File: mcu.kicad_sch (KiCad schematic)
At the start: 43 parts, among them J4 GPIO, J5 GND/3V3, Q3 MMBTA42, U4 STM32F103C8Tx, X1 SPI_DBG, X2 MTRBTN, X3 Bluetooth, X4 BuzzerHV, X5 BuzzerLV

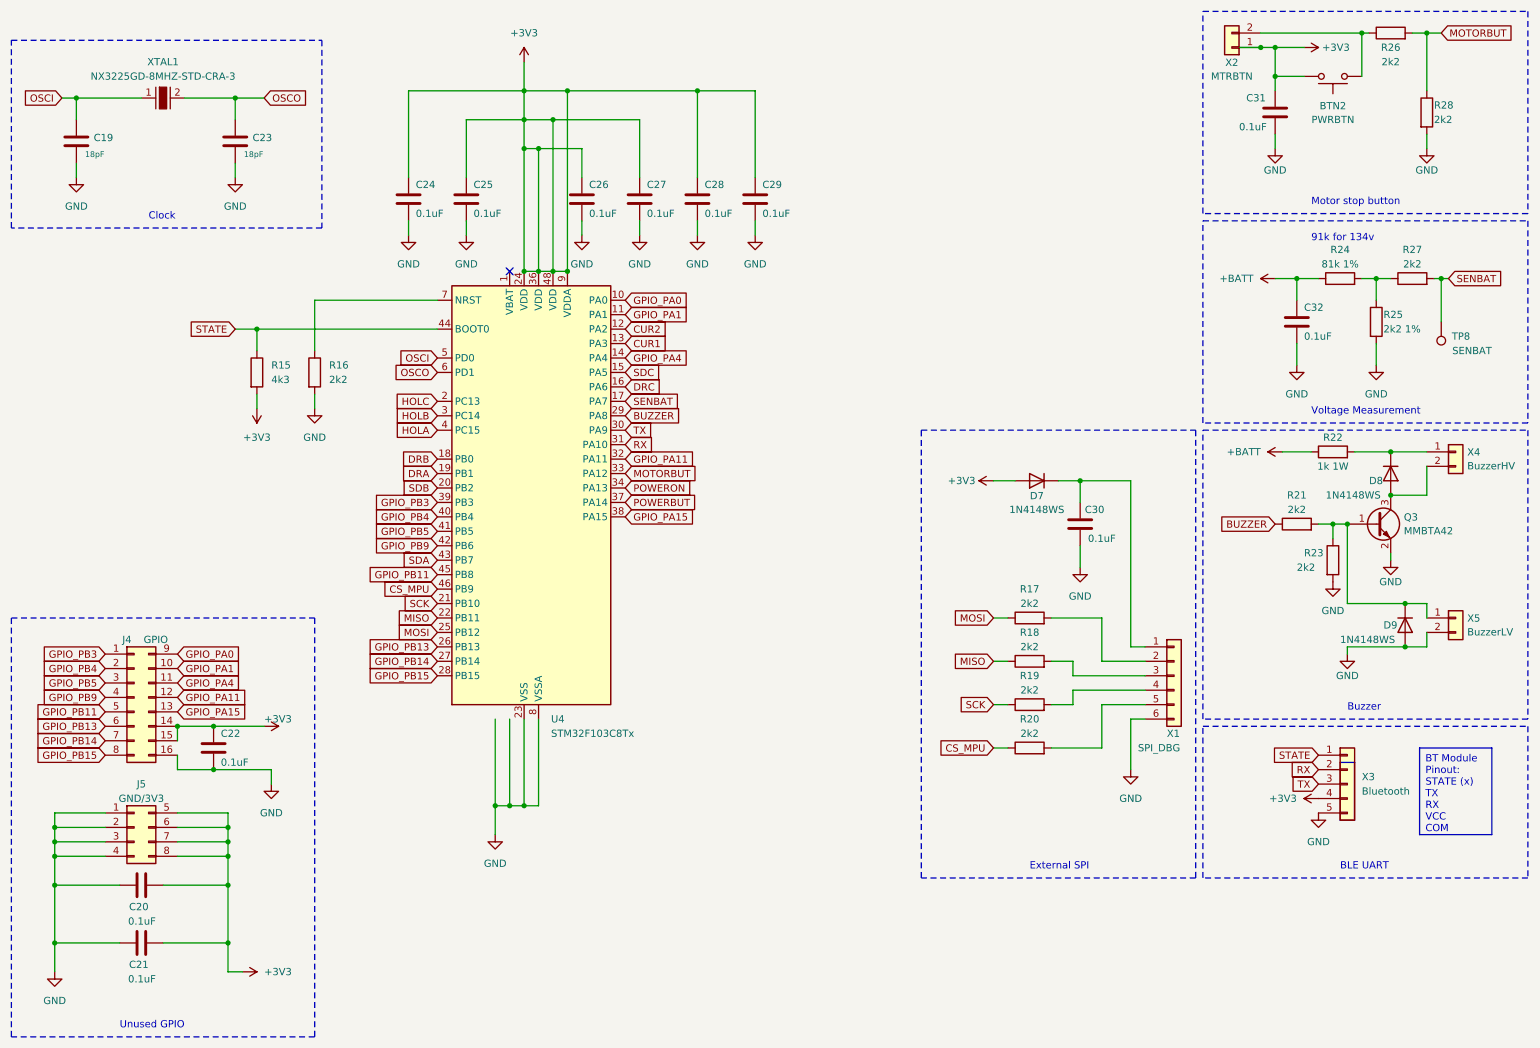
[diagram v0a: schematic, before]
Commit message: Add drivers, stepdown on VIPER115, fixes
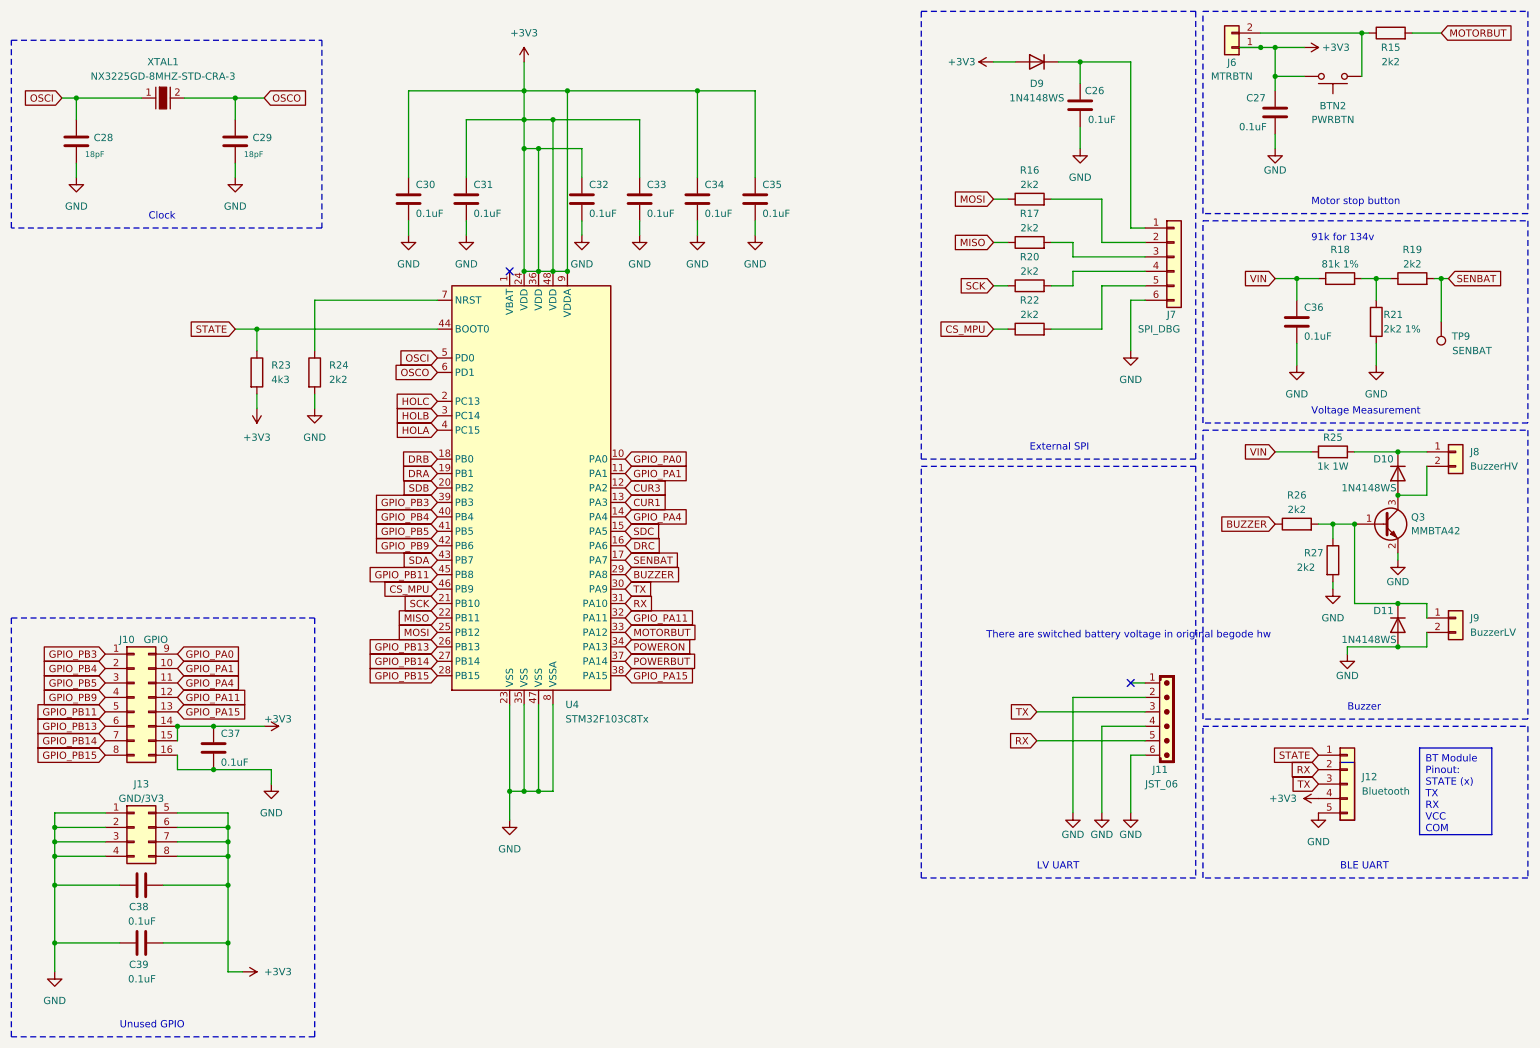
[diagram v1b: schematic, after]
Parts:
- removed D7, D8: 1N4148WS, Diode_SMD:D_SOD-323, symbol Diode:1N4148WS
- removed R28: 2k2, Resistor_SMD:R_0603_1608Metric_Pad0.98x0.95mm_HandSolder, symbol Device:R
- added D10, D11: 1N4148WS, Diode_SMD:D_SOD-323, symbol Diode:1N4148WS
- added J11: JST_06, Connector_JST:JST_EH_B6B-EH-A_1x06_P2.50mm_Vertical, symbol PCM_SL_Connectors:JST_06
- J12: renamed from X3; footprint (none) -> Connector_PinSocket_2.54mm:PinSocket_1x05_P2.54mm_Vertical
- J6: renamed from X2; footprint (none) -> Connector_JST:JST_XH_B2B-XH-A_1x02_P2.50mm_Vertical
- J7: renamed from X1; footprint (none) -> Connector_PinSocket_2.54mm:PinSocket_1x06_P2.54mm_Vertical
- J8: renamed from X4; footprint (none) -> Connector_JST:JST_XH_B2B-XH-A_1x02_P2.50mm_Vertical
- J9: renamed from X5; footprint (none) -> Connector_JST:JST_XH_B2B-XH-A_1x02_P2.50mm_Vertical
- renumbered C30 to C26, C31 to C27, C19 to C28, C23 to C29, C24 to C30, C25 to C31, C26 to C32, C27 to C33, C28 to C34, C29 to C35, C32 to C36, C22 to C37, C20 to C38, C21 to C39, J4 to J10, J5 to J13, R26 to R15, R17 to R16, R18 to R17, R24 to R18, R27 to R19, R19 to R20, R25 to R21, R20 to R22, R15 to R23, R16 to R24, R22 to R25, R21 to R26, R23 to R27, TP8 to TP9
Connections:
- net +3V3: now also D9.2 (A)
- net GND: now also D11.2 (A), J11.2, J11.4, J11.6; no longer D9.2 (A)
- net RX: now also J11.5
- net TX: now also J11.3
- net at C26.1, J7.1 (Pin_1): now also D9.1 (K)
- net at J8.1 (Pin_1), R25.2: now also D10.1 (K)
- net at J8.2 (Pin_2), Q3.3 (C): now also D10.2 (A)
- net at J9.1 (Pin_1), Q3.1 (B), R26.2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: now also D11.1 (K); no longer D9.1 (K)
- net +BATT renamed VIN
- net CUR2 renamed CUR3
- no-connect marks 1 -> 2
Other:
- note added: "LV UART"
- note added: "There are switched battery voltage in original begode hw"
- moved on the sheet: C26, J7, Q3, R16, R17, R20, R22

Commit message: topology in progress
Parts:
- added C57: 0.1uF, Capacitor_SMD:C_0805_2012Metric_Pad1.18x1.45mm_HandSolder, symbol Device:C
- C39: value 0.1uF -> 1uF
- R23: value 4k3 -> 4k7
- R25: value 1k 1W -> 1k5 1W
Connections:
- net +3V3: now also C57.1
- net GND: now also C57.2
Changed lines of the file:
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@@
   (junction (at 25.4 161.29) (diameter 0) (color 0 0 0 0)
   )
+  (junction (at 240.03 151.13) (diameter 0) (color 0 0 0 0)
+  )
   (junction (at 255.27 16.51) (diameter 0) (color 0 0 0 0)
   )
@@
   )
   (junction (at 25.4 158.75) (diameter 0) (color 0 0 0 0)
+  )
+  (junction (at 247.65 158.75) (diameter 0) (color 0 0 0 0)
   )
   (junction (at 29.21 27.94) (diameter 0) (color 0 0 0 0)
@@
     (stroke (width 0) (type default))
   )
+  (wire (pts (xy 240.03 158.75) (xy 247.65 158.75))
+    (stroke (width 0) (type default))
+  )
   (wire (pts (xy 25.4 153.67) (xy 25.4 156.21))
     (stroke (width 0) (type default))
@@
     (stroke (width 0) (type default))
   )
+  (wire (pts (xy 247.65 160.02) (xy 247.65 158.75))
+    (stroke (width 0) (type default))
+  )
   (wire (pts (xy 209.55 45.72) (xy 209.55 53.34))
     (stroke (width 0) (type default))
@@
     (stroke (width 0) (type default))
   )
+  (wire (pts (xy 247.65 158.75) (xy 247.65 153.67))
+    (stroke (width 0) (type default))
+  )
   (wire (pts (xy 25.4 181.61) (xy 25.4 176.53))
     (stroke (width 0) (type default))
@@
     (stroke (width 0) (type default))
   )
+  (wire (pts (xy 237.49 151.13) (xy 240.03 151.13))
+    (stroke (width 0) (type default))
+  )
   (wire (pts (xy 46.99 138.43) (xy 46.99 140.97))
     (stroke (width 0) (type default))
@@
   )
   (wire (pts (xy 55.88 181.61) (xy 55.88 176.53))
+    (stroke (width 0) (type default))
+  )
+  (wire (pts (xy 240.03 151.13) (xy 247.65 151.13))
     (stroke (width 0) (type default))
   )
@@
     (effects (font (size 1.27 1.27)) (justify left bottom))
   )
-  (text "There are switched battery voltage in original begode hw"
-    (at 189.23 123.19 0)
+  (text "There are switched battery voltage\nin original begode hw"
+    (at 190.5 130.81 0)
     (effects (font (size 1.27 1.27)) (justify left bottom))
   )
@@
     )
   )
-  (symbol (lib_id "power:GND") (at 247.65 153.67 0) (unit 1)
-    (in_bom yes) (on_board yes) (dnp no) (fields_autoplaced)
-    (property "Reference" "#PWR065" (at 247.65 160.02 0)
-      (effects (font (size 1.27 1.27)) hide)
-    )
-    (property "Value" "GND" (at 247.65 158.75 0)
-      (effects (font (size 1.27 1.27)))
-    )
-    (property "Footprint" "" (at 247.65 153.67 0)
-      (effects (font (size 1.27 1.27)) hide)
-    )
-    (property "Datasheet" "" (at 247.65 153.67 0)
+  (symbol (lib_id "power:GND") (at 247.65 160.02 0) (unit 1)
+    (in_bom yes) (on_board yes) (dnp no)
+    (property "Reference" "#PWR065" (at 247.65 166.37 0)
+      (effects (font (size 1.27 1.27)) hide)
+    )
+    (property "Value" "GND" (at 247.65 163.83 0)
+      (effects (font (size 1.27 1.27)))
+    )
+    (property "Footprint" "" (at 247.65 160.02 0)
+      (effects (font (size 1.27 1.27)) hide)
+    )
+    (property "Datasheet" "" (at 247.65 160.02 0)
       (effects (font (size 1.27 1.27)) hide)
     )
@@
       (effects (font (size 1.27 1.27)) (justify left))
     )
-    (property "Value" "4k3" (at 63.5 77.47 0)
+    (property "Value" "4k7" (at 63.5 77.47 0)
       (effects (font (size 1.27 1.27)) (justify left))
     )
@@
     )
   )
-  (symbol (lib_id "power:+3V3") (at 247.65 151.13 90) (unit 1)
+  (symbol (lib_id "power:+3V3") (at 237.49 151.13 90) (unit 1)
     (in_bom yes) (on_board yes) (dnp no) (fields_autoplaced)
-    (property "Reference" "#PWR061" (at 251.46 151.13 0)
-      (effects (font (size 1.27 1.27)) hide)
-    )
-    (property "Value" "+3V3" (at 243.84 151.13 90)
-      (effects (font (size 1.27 1.27)) (justify left))
-    )
-    (property "Footprint" "" (at 247.65 151.13 0)
-      (effects (font (size 1.27 1.27)) hide)
-    )
-    (property "Datasheet" "" (at 247.65 151.13 0)
+    (property "Reference" "#PWR061" (at 241.3 151.13 0)
+      (effects (font (size 1.27 1.27)) hide)
+    )
+    (property "Value" "+3V3" (at 233.68 151.13 90)
+      (effects (font (size 1.27 1.27)) (justify left))
+    )
+    (property "Footprint" "" (at 237.49 151.13 0)
+      (effects (font (size 1.27 1.27)) hide)
+    )
+    (property "Datasheet" "" (at 237.49 151.13 0)
       (effects (font (size 1.27 1.27)) hide)
     )
@@
         (path "/c57bc97c-1c43-4bb1-9424-fed846030b7b/013bb254-f239-4c32-8f76-0a97895c10b6"
           (reference "#PWR061") (unit 1)
+        )
+      )
+    )
+  )
+  (symbol (lib_id "Device:C") (at 240.03 154.94 0) (unit 1)
+    (in_bom yes) (on_board yes) (dnp no)
+    (property "Reference" "C57" (at 241.3 152.4 0)
+      (effects (font (size 1.27 1.27)) (justify left))
+    )
+    (property "Value" "0.1uF" (at 241.3 157.48 0)
+      (effects (font (size 1.27 1.27)) (justify left))
+    )
+    (property "Footprint" "Capacitor_SMD:C_0805_2012Metric_Pad1.18x1.45mm_HandSolder" (at 240.9952 158.75 0)
+      (effects (font (size 1.27 1.27)) hide)
+    )
+    (property "Datasheet" "~" (at 240.03 154.94 0)
+      (effects (font (size 1.27 1.27)) hide)
+    )
+    (pin "1")
+    (pin "2")
+    (instances
+      (project "ShiftWay_f103"
+        (path "/c57bc97c-1c43-4bb1-9424-fed846030b7b/013bb254-f239-4c32-8f76-0a97895c10b6"
+          (reference "C57") (unit 1)
         )
       )
@@
       (effects (font (size 1.27 1.27)) (justify left))
     )
-    (property "Value" "0.1uF" (at 43.18 182.88 90)
+    (property "Value" "1uF" (at 43.18 182.88 90)
       (effects (font (size 1.27 1.27)) (justify left))
     )
@@
       (effects (font (size 1.27 1.27)))
     )
-    (property "Value" "1k 1W" (at 250.19 92.71 90)
-      (effects (font (size 1.27 1.27)))
-    )
+    (property "Value" "1k5 1W" (at 250.19 92.71 90)
+      (effects (font (size 1.27 1.27)))
+    )

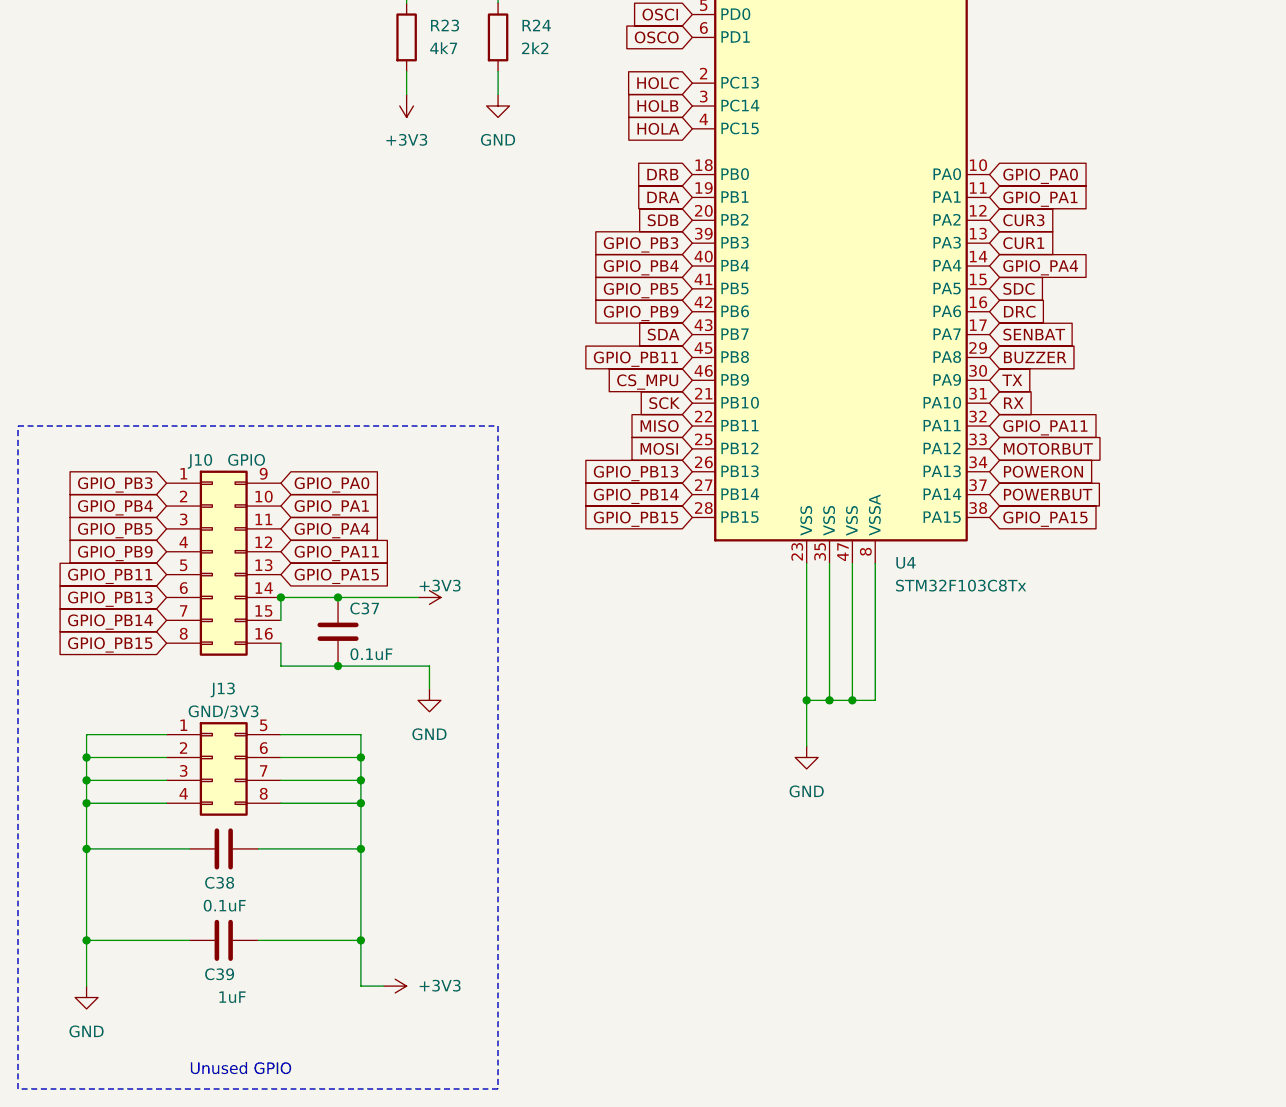
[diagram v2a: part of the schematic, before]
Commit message: Replaced unused GPIO, added SWD connectorm, PCB in progress
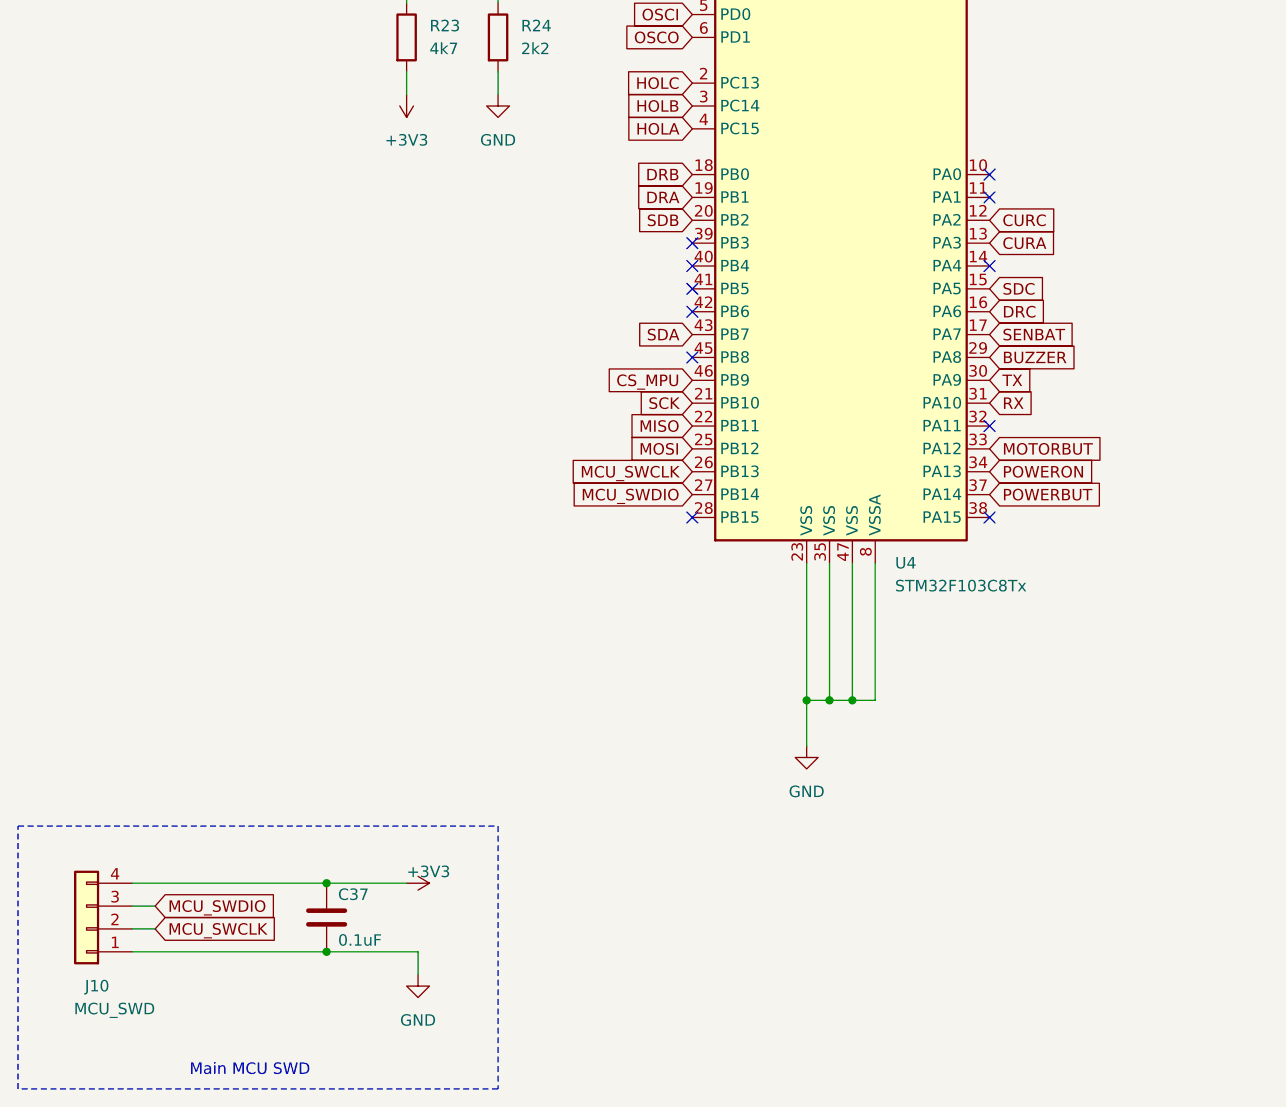
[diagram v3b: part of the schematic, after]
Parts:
- removed C38: 0.1uF, Capacitor_SMD:C_0603_1608Metric_Pad1.08x0.95mm_HandSolder, symbol Device:C
- removed C39: 1uF, Capacitor_SMD:C_0603_1608Metric_Pad1.08x0.95mm_HandSolder, symbol Device:C
- removed J10: GPIO, Connector_PinSocket_2.54mm:PinSocket_2x08_P2.54mm_Vertical, symbol Connector_Generic:Conn_02x08_Top_Bottom
- removed J13: GND/3V3, Connector_PinSocket_2.54mm:PinSocket_2x04_P2.54mm_Vertical, symbol Connector_Generic:Conn_02x04_Top_Bottom
- added J10: MCU_SWD, Connector_PinSocket_2.54mm:PinSocket_1x04_P2.54mm_Vertical, symbol Connector_Generic:Conn_01x04
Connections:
- net +3V3: now also J10.4 (Pin_4)
- net GND: now also J10.1 (Pin_1)
- net CUR1 renamed CURA
- net CUR3 renamed CURC
- net GPIO_PA0: no longer names the net of U4.10 (PA0)
- net GPIO_PA1: no longer names the net of U4.11 (PA1)
- net GPIO_PA11: no longer names the net of U4.32 (PA11)
- net GPIO_PA15: no longer names the net of U4.38 (PA15)
- net GPIO_PA4: no longer names the net of U4.14 (PA4)
- net GPIO_PB11: no longer names the net of U4.45 (PB8)
- net GPIO_PB13 renamed MCU_SWCLK
- net MCU_SWCLK: now also J10.2 (Pin_2)
- net GPIO_PB14 renamed MCU_SWDIO
- net MCU_SWDIO: now also J10.3 (Pin_3)
- net GPIO_PB15: no longer names the net of U4.28 (PB15)
- net GPIO_PB3: no longer names the net of U4.39 (PB3)
- net GPIO_PB4: no longer names the net of U4.40 (PB4)
- net GPIO_PB5: no longer names the net of U4.41 (PB5)
- net GPIO_PB9: no longer names the net of U4.42 (PB6)
- no-connect marks 2 -> 13
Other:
- note added: "Main MCU SWD"
- note removed: "Unused GPIO"
- moved on the sheet: C37

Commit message: Fixes, layouting
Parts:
- C57: footprint Capacitor_SMD:C_0805_2012Metric_Pad1.18x1.45mm_HandSolder -> Capacitor_SMD:C_0603_1608Metric_Pad1.08x0.95mm_HandSolder
- J7: footprint Connector_PinSocket_2.54mm:PinSocket_1x06_P2.54mm_Vertical -> Connector_PinSocket_1.27mm:PinSocket_1x07_P1.27mm_Vertical
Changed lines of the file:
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@@
       (effects (font (size 1.27 1.27)) (justify left))
     )
-    (property "Footprint" "Capacitor_SMD:C_0805_2012Metric_Pad1.18x1.45mm_HandSolder" (at 240.9952 158.75 0)
+    (property "Footprint" "Capacitor_SMD:C_0603_1608Metric_Pad1.08x0.95mm_HandSolder" (at 240.9952 158.75 0)
       (effects (font (size 1.27 1.27)) hide)
     )
@@
       (effects (font (size 1.27 1.27)) (justify left))
     )
-    (property "Footprint" "Connector_PinSocket_2.54mm:PinSocket_1x06_P2.54mm_Vertical" (at 222.25 55.88 0)
-      (effects (font (size 1.27 1.27)) hide)
-    )
+    (property "Footprint" "Connector_PinSocket_1.27mm:PinSocket_1x07_P1.27mm_Vertical" (at 222.25 55.88 0)
+      (effects (font (size 1.27 1.27)) hide)
+    )
